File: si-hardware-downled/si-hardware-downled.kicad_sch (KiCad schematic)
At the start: 19 parts, among them U1 BP2866D, U2 S4525S

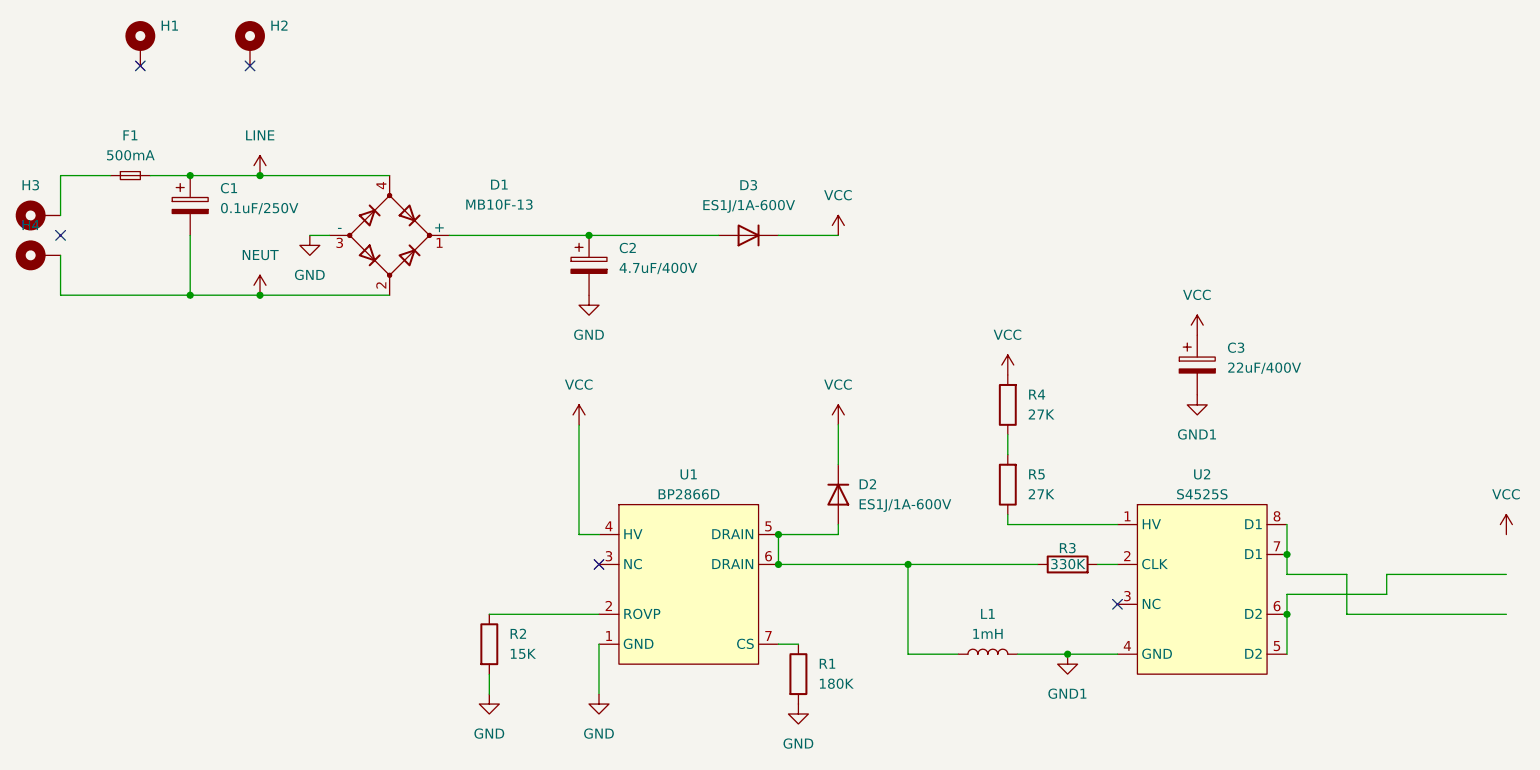
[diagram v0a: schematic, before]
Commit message: change inductor choke filter
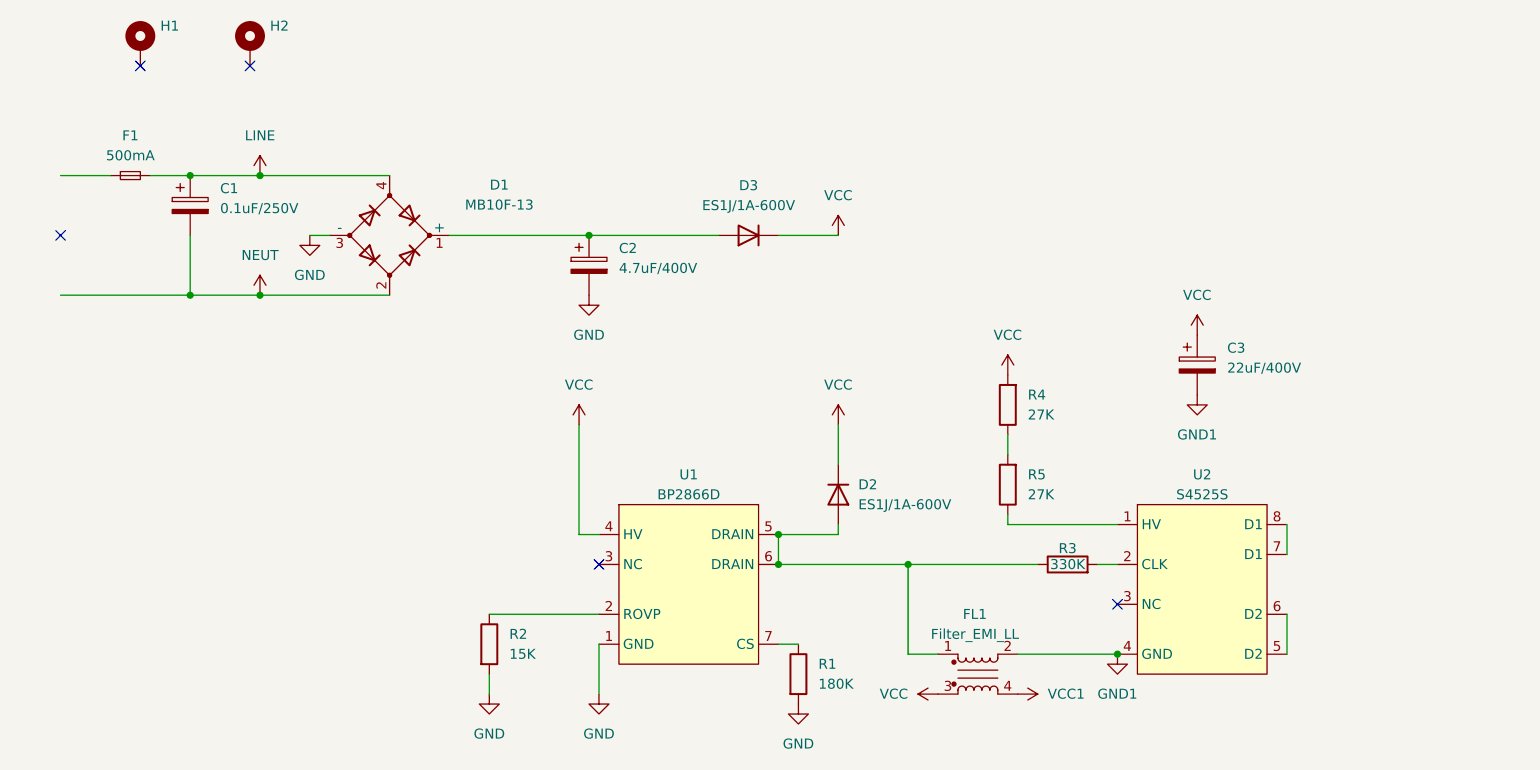
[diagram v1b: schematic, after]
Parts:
- removed H3, H4: MountingHole_Pad_MP, MountingHole:MountingHole_3.2mm_M3_DIN965_Pad, symbol Mechanical:MountingHole_Pad_MP
- removed L1: 1mH, Inductor_SMD:L_Chilisin_BMRF00101040, symbol Device:L
- added FL1: Filter_EMI_LL, Inductor_THT:L_CommonMode_Wuerth_WE-CMB-M, symbol Device:Filter_EMI_LL
- C1: Order (none) -> https://dientutuyetnga.com/products/tu-104-275v-0-1uf
- C2: Order (none) -> https://dientutuyetnga.com/products/tu-hoa-4-7uf-250v
- D1: Order (none) -> https://www.thegioiic.com/mb10f-diode-cau-chinh-luu-1kv-0-5a
- D2, D3: Order (none) -> https://www.thegioiic.com/es1j-sma-diode-chinh-luu-1a-600v
- F1: Order (none) -> https://dientutuyetnga.com/products/1808-cau-chi-500ma-250v
- R1: Orde (none) -> https://www.thegioiic.com/dien-tro-180-kohm-0805-1-
- R2: Order (none) -> https://www.thegioiic.com/dien-tro-15-kohm-1206-5-
- R3: Order (none) -> https://dientutuyetnga.com/products/dien-tro-330k-0805-1
- R4, R5: Order (none) -> https://dientutuyetnga.com/products/dien-tro-27k-1206-1
- U1: Order (none) -> https://linhkienhatech.com/products/linh-kien-ic-driver-led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
- U2: Order (none) -> https://id.aliexpress.com/i/1005006071957980.html?gatewayAd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
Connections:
- net GND1: now also FL1.2
- net VCC: now also FL1.3
- net at D2.2 (A), R3.1, U1.5 (DRAIN)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: now also FL1.1
- new net VCC1: FL1.4

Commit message: export file gerber + drill
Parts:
- C2: footprint Capacitor_THT:C_Radial_D5.0mm_H11.0mm_P2.00mm -> Capacitor_THT:C_Radial_D8.0mm_H11.5mm_P3.50mm
- C3: footprint Capacitor_THT:C_Radial_D5.0mm_H11.0mm_P2.00mm -> Capacitor_THT:C_Radial_D12.5mm_H20.0mm_P5.00mm; Order (none) -> https://www.thegioiic.com/tu-hoa-22uf-400v-13x21mm-xuyen-lo
- FL1: value Filter_EMI_LL -> 10mH; footprint Inductor_THT:L_CommonMode_Wuerth_WE-CMB-M -> QSL_Filter:choke_4pin_7x8; Order (none) -> https://www.thegioiic.com/cuon-cam-10mh-uu9-8-103
- R1: Orde https://www.thegioiic.com/dien-tro-180-kohm-0805-1- -> (none); Order (none) -> https://www.thegioiic.com/dien-tro-180-kohm-0805-1-
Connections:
- net VCC: no longer C3.1
- net VCC1: now also C3.1
- no-connect marks 5 -> 4
